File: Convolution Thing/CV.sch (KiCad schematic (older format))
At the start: 8 parts

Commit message: Better CV inputs, LED driver, display & USB interfaces
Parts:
- removed J?: CV Header, symbol Connector:Conn_01x08_Female
- added C? (x8): 330pF, symbol Device:C
- added C? (x4): 100nF, symbol Device:C
- added C? (x8): 2nF, symbol Device:C
- added J?: CV Header, symbol Connector:Conn_01x09_Female
- added R? (x8): 3k, symbol Device:R
- added R? (x8): 1.2k, symbol Device:R
- added R? (x2): 2k, symbol Device:R
- added R? (x8): 50, symbol Device:R
- added U? (x10): MCP6004, symbol Amplifier_Operational:MCP6004
- added U? (x2): LM4040DBZ-2.0, Package_TO_SOT_SMD:SOT-23, symbol Reference_Voltage:LM4040DBZ-2.0
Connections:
- net labels added: +12V, +5VA, -12V, CV_IN_1, CV_IN_2, CV_IN_3, CV_IN_4, CV_IN_5, CV_IN_6, CV_IN_7, CV_IN_8, VREF_-2.048
- net labels removed: CV_VREF
- wire segments 15 -> 170
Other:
- note added: "Bipolar sampling"
- note removed: "Unipolar sampling"
- moved on the sheet: C?

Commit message: Added gate inputs and CM4 / display sockets, made CV inputs 100k, lots of smaller changes. First iteration of schematic now done.
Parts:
- removed C?: 2.2uF, symbol Device:C
- removed C? (x7): 330pF, symbol Device:C
- removed C? (x7): 2nF, symbol Device:C
- removed J?: CV Header, symbol Connector:Conn_01x09_Female
- removed R? (x7): 3k, symbol Device:R
- removed R? (x7): 1.2k, symbol Device:R
- removed R? (x7): 50, symbol Device:R
- removed U? (x2): LM4040DBZ-2.0, Package_TO_SOT_SMD:SOT-23, symbol Reference_Voltage:LM4040DBZ-2.0
- removed U? (x7): MCP6004, symbol Amplifier_Operational:MCP6004
- added C? (x7): 330pF, symbol Device:C
- added C? (x7): 2nF, symbol Device:C
- added J?: In CV 1, symbol Connector:AudioJack2_SwitchT
- added J?: In CV 2, symbol Connector:AudioJack2_SwitchT
- added J?: In CV 3, symbol Connector:AudioJack2_SwitchT
- added J?: In CV 6, symbol Connector:AudioJack2_SwitchT
- added J?: In CV 5, symbol Connector:AudioJack2_SwitchT
- added J?: In CV 4, symbol Connector:AudioJack2_SwitchT
- added J?: In CV 7, symbol Connector:AudioJack2_SwitchT
- added J?: In CV 8, symbol Connector:AudioJack2_SwitchT
- added R? (x15): 50k, symbol Device:R
- added R? (x7): 100k, symbol Device:R
- added R? (x7): 47, symbol Device:R
- added TP?: CV1 TP, symbol Connector:TestPoint
- added TP?: +2.5V TP, symbol Connector:TestPoint
- added TP?: -2.5V TP, symbol Connector:TestPoint
- added U? (x2): LM4040DBZ-2.5, Package_TO_SOT_SMD:SOT-23, symbol Reference_Voltage:LM4040DBZ-2.5
- added U? (x7): MCP6004, symbol Amplifier_Operational:MCP6004
- R?: value 3k -> 100k
- R?: value 1.2k -> 50k
- R?: value 50 -> 47
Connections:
- net labels added: VREF_-2.5
- net labels removed: CV_IN_1, CV_IN_2, CV_IN_3, CV_IN_4, CV_IN_5, CV_IN_6, CV_IN_7, CV_IN_8, VREF_-2.048
- wire segments 170 -> 171
- no-connect marks 0 -> 8
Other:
- note added: "3mA"
- moved on the sheet: C?, R?, U?A, U?E

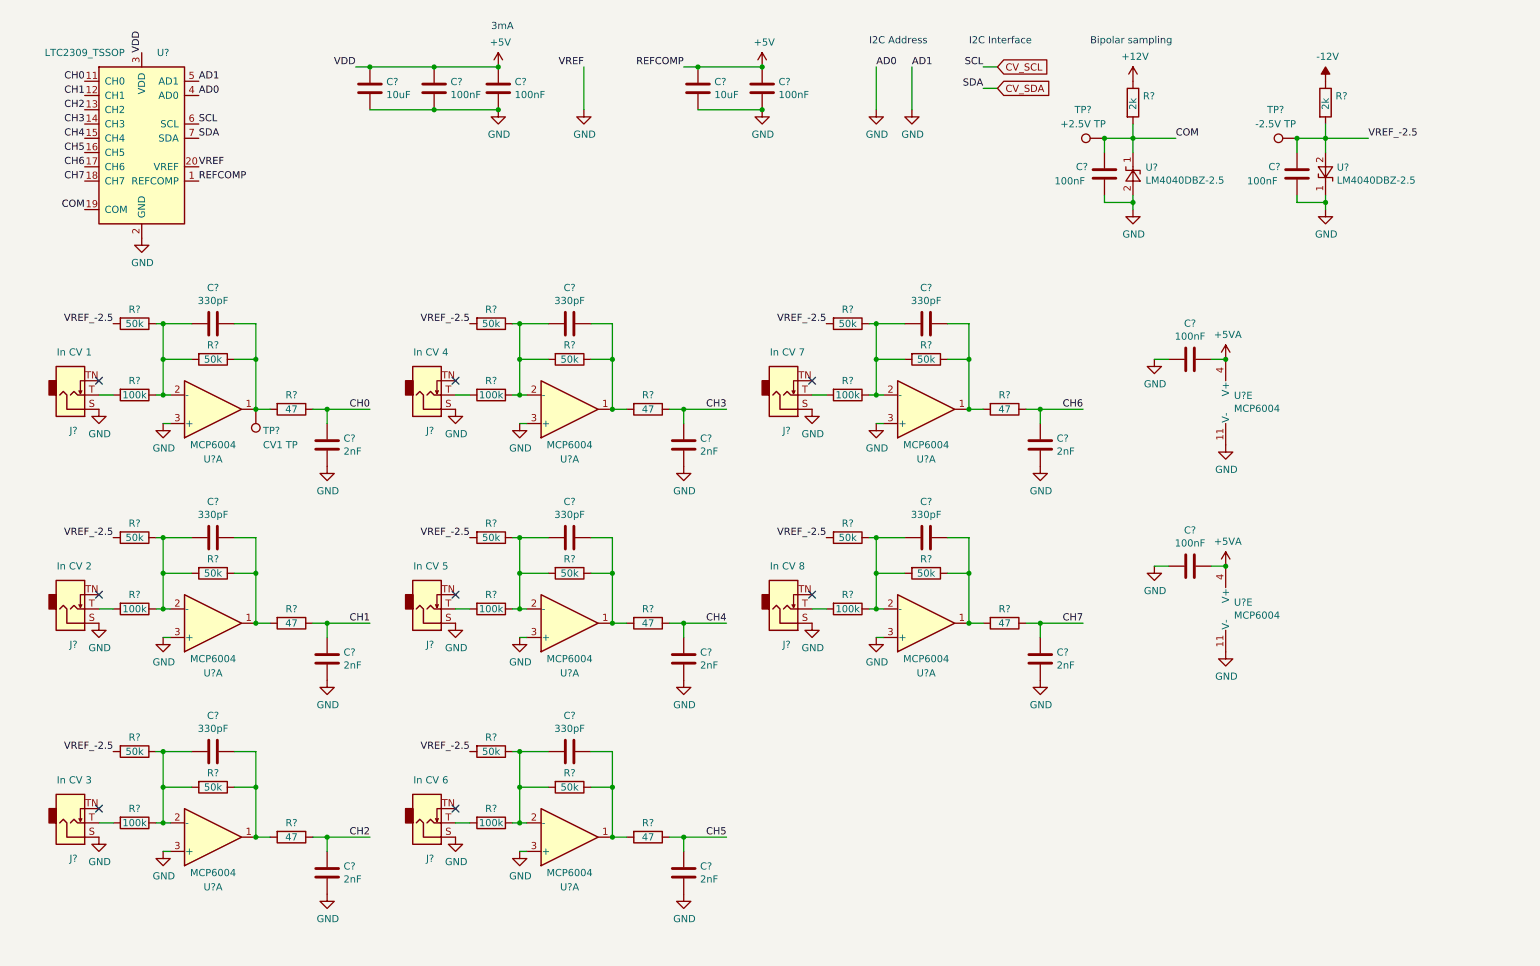
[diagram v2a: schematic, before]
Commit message: Fix some issues, add component references
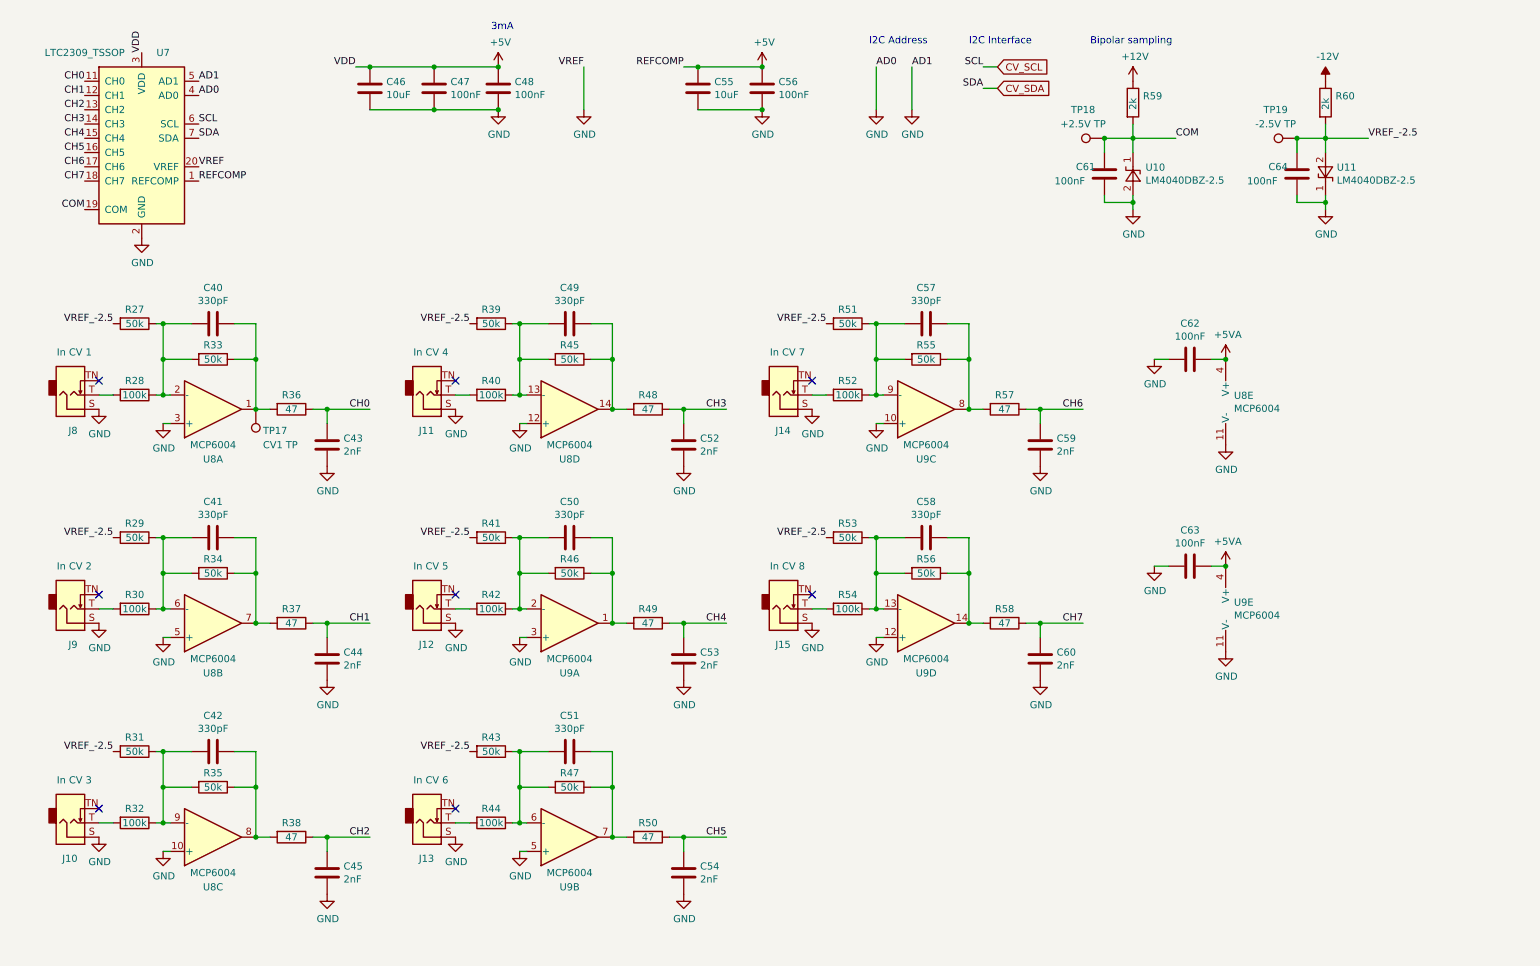
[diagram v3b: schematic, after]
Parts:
- gave numbers to parts that had none: 75
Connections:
- net GND: now also U8.10 (+), U8.12 (+), U8.5 (+), U9.10 (+), U9.12 (+), U9.5 (+); no longer U8.3 (+), U8.3 (+), U8.3 (+), U9.3 (+), U9.3 (+), U9.3 (+)
- net at C41.1, R34.1, R37.2: now also U8.7; no longer U8.1
- net at C41.2, R29.1, R30.1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: now also U8.6 (-); no longer U8.2 (-)
- net at C42.1, R35.1, R38.2: now also U8.8; no longer U8.1
- net at C42.2, R31.1, R32.1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: now also U8.9 (-); no longer U8.2 (-)
- net at C49.1, R45.1, R48.2: now also U8.14; no longer U8.1
- net at C49.2, R39.1, R40.1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: now also U8.13 (-); no longer U8.2 (-)
- net at C51.1, R47.1, R50.2: now also U9.7; no longer U9.1
- net at C51.2, R43.1, R44.1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: now also U9.6 (-); no longer U9.2 (-)
- net at C57.1, R55.1, R57.2: now also U9.8; no longer U9.1
- net at C57.2, R51.1, R52.1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: now also U9.9 (-); no longer U9.2 (-)
- net at C58.1, R56.1, R58.2: now also U9.14; no longer U9.1
- net at C58.2, R53.1, R54.1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: now also U9.13 (-); no longer U9.2 (-)

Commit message: Assign all footprints
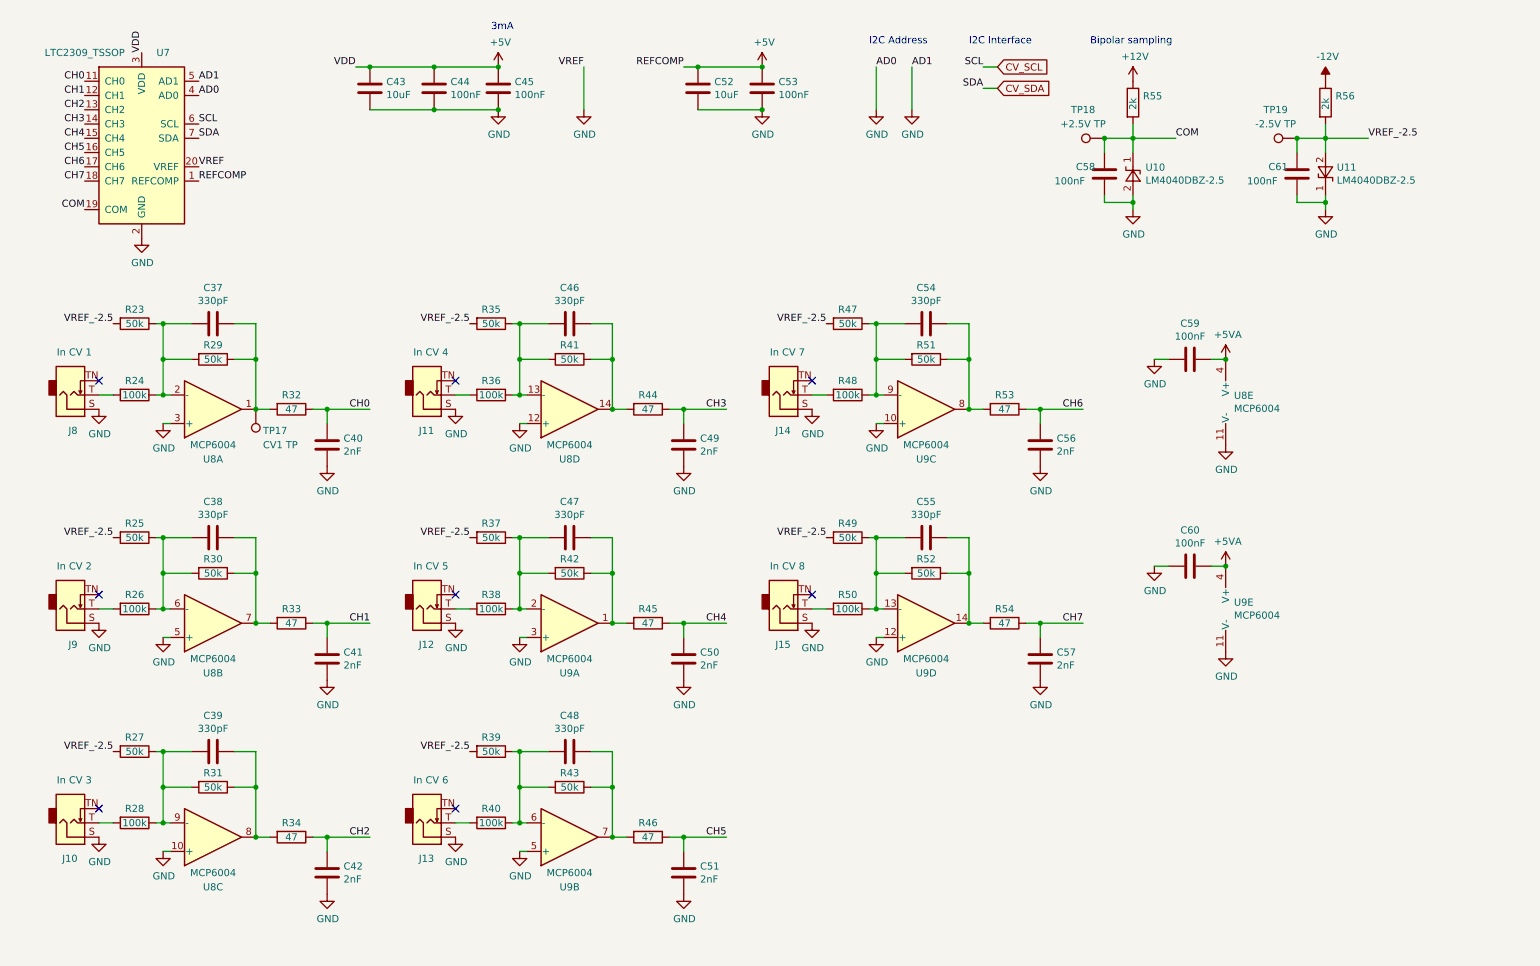
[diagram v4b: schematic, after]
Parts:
- C37: renamed from C40; footprint (none) -> Capacitor_SMD:C_0805_2012Metric
- C38: renamed from C41; footprint (none) -> Capacitor_SMD:C_0805_2012Metric
- C39: renamed from C42; footprint (none) -> Capacitor_SMD:C_0805_2012Metric
- C40: renamed from C43; footprint (none) -> Capacitor_SMD:C_0805_2012Metric
- C41: renamed from C44; footprint (none) -> Capacitor_SMD:C_0805_2012Metric
- C42: renamed from C45; footprint (none) -> Capacitor_SMD:C_0805_2012Metric
- C43: renamed from C46; footprint (none) -> Capacitor_SMD:C_0805_2012Metric
- C44: renamed from C47; footprint (none) -> Capacitor_SMD:C_0805_2012Metric
- C45: renamed from C48; footprint (none) -> Capacitor_SMD:C_0805_2012Metric
- C46: renamed from C49; footprint (none) -> Capacitor_SMD:C_0805_2012Metric
- C47: renamed from C50; footprint (none) -> Capacitor_SMD:C_0805_2012Metric
- C48: renamed from C51; footprint (none) -> Capacitor_SMD:C_0805_2012Metric
- C49: renamed from C52; footprint (none) -> Capacitor_SMD:C_0805_2012Metric
- C50: renamed from C53; footprint (none) -> Capacitor_SMD:C_0805_2012Metric
- C51: renamed from C54; footprint (none) -> Capacitor_SMD:C_0805_2012Metric
- C52: renamed from C55; footprint (none) -> Capacitor_SMD:C_0805_2012Metric
- C53: renamed from C56; footprint (none) -> Capacitor_SMD:C_0805_2012Metric
- C54: renamed from C57; footprint (none) -> Capacitor_SMD:C_0805_2012Metric
- C55: renamed from C58; footprint (none) -> Capacitor_SMD:C_0805_2012Metric
- C56: renamed from C59; footprint (none) -> Capacitor_SMD:C_0805_2012Metric
- C57: renamed from C60; footprint (none) -> Capacitor_SMD:C_0805_2012Metric
- C58: renamed from C61; footprint (none) -> Capacitor_SMD:C_0805_2012Metric
- C59: renamed from C62; footprint (none) -> Capacitor_SMD:C_0805_2012Metric
- C60: renamed from C63; footprint (none) -> Capacitor_SMD:C_0805_2012Metric
- C61: renamed from C64; footprint (none) -> Capacitor_SMD:C_0805_2012Metric
- J10, J11, J12, J13, J14, J15, J8, J9: footprint (none) -> SamacSys:ACJMNV352S
- R23: renamed from R27; footprint (none) -> Resistor_SMD:R_0805_2012Metric
- R24: renamed from R28; footprint (none) -> Resistor_SMD:R_0805_2012Metric
- R25: renamed from R29; footprint (none) -> Resistor_SMD:R_0805_2012Metric
- R26: renamed from R30; footprint (none) -> Resistor_SMD:R_0805_2012Metric
- R27: renamed from R31; footprint (none) -> Resistor_SMD:R_0805_2012Metric
- R28: renamed from R32; footprint (none) -> Resistor_SMD:R_0805_2012Metric
- R29: renamed from R33; footprint (none) -> Resistor_SMD:R_0805_2012Metric
- R30: renamed from R34; footprint (none) -> Resistor_SMD:R_0805_2012Metric
- R31: renamed from R35; footprint (none) -> Resistor_SMD:R_0805_2012Metric
- R32: renamed from R36; footprint (none) -> Resistor_SMD:R_0805_2012Metric
- R33: renamed from R37; footprint (none) -> Resistor_SMD:R_0805_2012Metric
- R34: renamed from R38; footprint (none) -> Resistor_SMD:R_0805_2012Metric
- R35: renamed from R39; footprint (none) -> Resistor_SMD:R_0805_2012Metric
- R36: renamed from R40; footprint (none) -> Resistor_SMD:R_0805_2012Metric
- R37: renamed from R41; footprint (none) -> Resistor_SMD:R_0805_2012Metric
- R38: renamed from R42; footprint (none) -> Resistor_SMD:R_0805_2012Metric
- R39: renamed from R43; footprint (none) -> Resistor_SMD:R_0805_2012Metric
- R40: renamed from R44; footprint (none) -> Resistor_SMD:R_0805_2012Metric
- R41: renamed from R45; footprint (none) -> Resistor_SMD:R_0805_2012Metric
- R42: renamed from R46; footprint (none) -> Resistor_SMD:R_0805_2012Metric
- R43: renamed from R47; footprint (none) -> Resistor_SMD:R_0805_2012Metric
- R44: renamed from R48; footprint (none) -> Resistor_SMD:R_0805_2012Metric
- R45: renamed from R49; footprint (none) -> Resistor_SMD:R_0805_2012Metric
- R46: renamed from R50; footprint (none) -> Resistor_SMD:R_0805_2012Metric
- R47: renamed from R51; footprint (none) -> Resistor_SMD:R_0805_2012Metric
- R48: renamed from R52; footprint (none) -> Resistor_SMD:R_0805_2012Metric
- R49: renamed from R53; footprint (none) -> Resistor_SMD:R_0805_2012Metric
- R50: renamed from R54; footprint (none) -> Resistor_SMD:R_0805_2012Metric
- R51: renamed from R55; footprint (none) -> Resistor_SMD:R_0805_2012Metric
- R52: renamed from R56; footprint (none) -> Resistor_SMD:R_0805_2012Metric
- R53: renamed from R57; footprint (none) -> Resistor_SMD:R_0805_2012Metric
- R54: renamed from R58; footprint (none) -> Resistor_SMD:R_0805_2012Metric
- R55: renamed from R59; footprint (none) -> Resistor_SMD:R_0805_2012Metric
- R56: renamed from R60; footprint (none) -> Resistor_SMD:R_0805_2012Metric
- TP17, TP18, TP19: footprint (none) -> TestPoint:TestPoint_Loop_D2.60mm_Drill1.6mm_Beaded
- U8, U9: footprint (none) -> Package_SO:SOIC-14_3.9x8.7mm_P1.27mm

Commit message: PCB layout work and related changes to the schematic
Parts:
- removed C52: 10uF, Capacitor_SMD:C_0805_2012Metric, symbol Device:C
- removed C53: 100nF, Capacitor_SMD:C_0805_2012Metric, symbol Device:C
- added TP13: CV1 TP, TestPoint:TestPoint_Loop_D2.60mm_Drill1.6mm_Beaded, symbol Connector:TestPoint
- added TP14: CV2 TP, TestPoint:TestPoint_Loop_D2.60mm_Drill1.6mm_Beaded, symbol Connector:TestPoint
- added TP15: CV3 TP, TestPoint:TestPoint_Loop_D2.60mm_Drill1.6mm_Beaded, symbol Connector:TestPoint
- added TP16: CV4 TP, TestPoint:TestPoint_Loop_D2.60mm_Drill1.6mm_Beaded, symbol Connector:TestPoint
- added TP18: CV6 TP, TestPoint:TestPoint_Loop_D2.60mm_Drill1.6mm_Beaded, symbol Connector:TestPoint
- added TP19: CV_SCL TP, TestPoint:TestPoint_Loop_D2.60mm_Drill1.6mm_Beaded, symbol Connector:TestPoint
- added TP20: CV_SDA TP, TestPoint:TestPoint_Loop_D2.60mm_Drill1.6mm_Beaded, symbol Connector:TestPoint
- added TP21: CV7 TP, TestPoint:TestPoint_Loop_D2.60mm_Drill1.6mm_Beaded, symbol Connector:TestPoint
- added TP22: CV8 TP, TestPoint:TestPoint_Loop_D2.60mm_Drill1.6mm_Beaded, symbol Connector:TestPoint
- J10: renamed from J11; footprint SamacSys:ACJMNV352S -> Connector_Audio:Jack_3.5mm_QingPu_WQP-PJ398SM_Vertical_CircularHoles
- J11: renamed from J12; footprint SamacSys:ACJMNV352S -> Connector_Audio:Jack_3.5mm_QingPu_WQP-PJ398SM_Vertical_CircularHoles
- J12: renamed from J13; footprint SamacSys:ACJMNV352S -> Connector_Audio:Jack_3.5mm_QingPu_WQP-PJ398SM_Vertical_CircularHoles
- J13: renamed from J14; footprint SamacSys:ACJMNV352S -> Connector_Audio:Jack_3.5mm_QingPu_WQP-PJ398SM_Vertical_CircularHoles
- J14: renamed from J15; footprint SamacSys:ACJMNV352S -> Connector_Audio:Jack_3.5mm_QingPu_WQP-PJ398SM_Vertical_CircularHoles
- J7: renamed from J8; footprint SamacSys:ACJMNV352S -> Connector_Audio:Jack_3.5mm_QingPu_WQP-PJ398SM_Vertical_CircularHoles
- J8: renamed from J9; footprint SamacSys:ACJMNV352S -> Connector_Audio:Jack_3.5mm_QingPu_WQP-PJ398SM_Vertical_CircularHoles
- J9: renamed from J10; footprint SamacSys:ACJMNV352S -> Connector_Audio:Jack_3.5mm_QingPu_WQP-PJ398SM_Vertical_CircularHoles
- TP17: value CV1 TP -> CV5 TP
- renumbered C37 to C33, C38 to C34, C39 to C35, C40 to C36, C41 to C37, C42 to C38, C43 to C39, C44 to C40, C45 to C41, C46 to C42, C47 to C43, C48 to C44, C49 to C45, C50 to C46, C51 to C47, C54 to C50, C55 to C51, C56 to C52, C57 to C53, C59 to C54, C60 to C55, C58 to C56, C61 to C57, R23 to R21, R24 to R22, R25 to R23, R26 to R24, R27 to R25, R28 to R26, R29 to R27, R30 to R28, R31 to R29, R32 to R30, R33 to R31, R34 to R32, R35 to R33, R36 to R34, R37 to R35, R38 to R36, R39 to R37, R40 to R38, R41 to R39, R42 to R40, R43 to R41, R44 to R42, R45 to R43, R46 to R44, R47 to R45, R48 to R46, R49 to R47, R50 to R48, R51 to R49, R52 to R50, R53 to R51, R54 to R52, R55 to R53, R56 to R54, TP18 to TP23, TP19 to TP24, U7 to U5, U8 to U6, U9 to U7, U10 to U8, U11 to U9
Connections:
- net CH0: now also TP13.1
- net CH1: now also TP14.1
- net CH2: now also TP15.1
- net CH3: now also TP16.1
- net CH4: now also TP17.1
- net CH5: now also TP18.1
- net CH6: now also TP21.1
- net CH7: now also TP22.1
- net at C33.1, R27.1, R30.2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: no longer TP17.1
- net CV_SCL renamed CM4_SCL3
- net CM4_SCL3: now also TP19.1
- net CV_SDA renamed CM4_SDA3
- net CM4_SDA3: now also TP20.1
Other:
- moved on the sheet: C56, C57, R53, R54, TP23, TP24, U8, U9
